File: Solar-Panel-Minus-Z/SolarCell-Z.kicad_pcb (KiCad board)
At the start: 6 copper layers, 48.4 x 48.4 mm, 74 parts, among them J1 XF2M-1015-1A, J2 U.FL-R-SMT-1, Q1 IRLML2803, U1 NDS8434, U2 Value, U3 Value, U4 TTB12G51-Balun

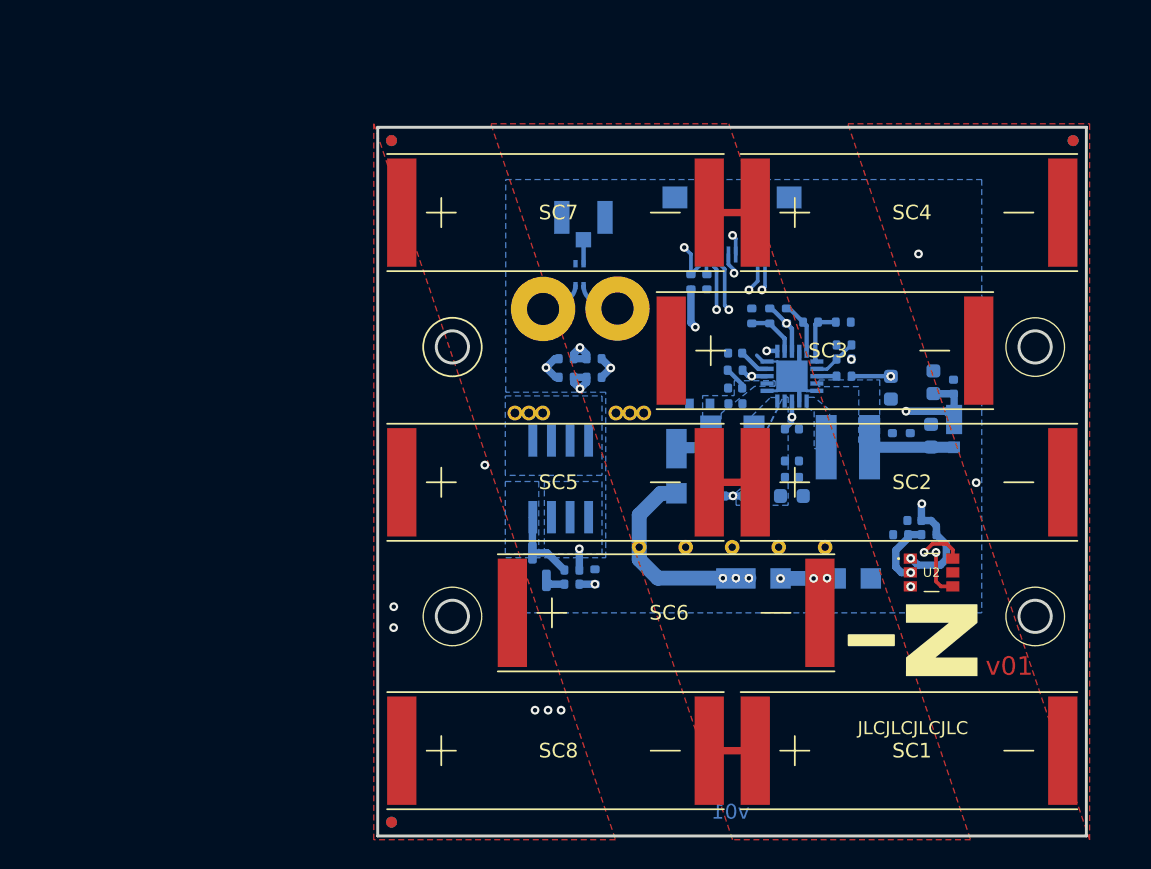
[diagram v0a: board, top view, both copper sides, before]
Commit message: Done with X, +/-Y, and +Z. TODO: -Z
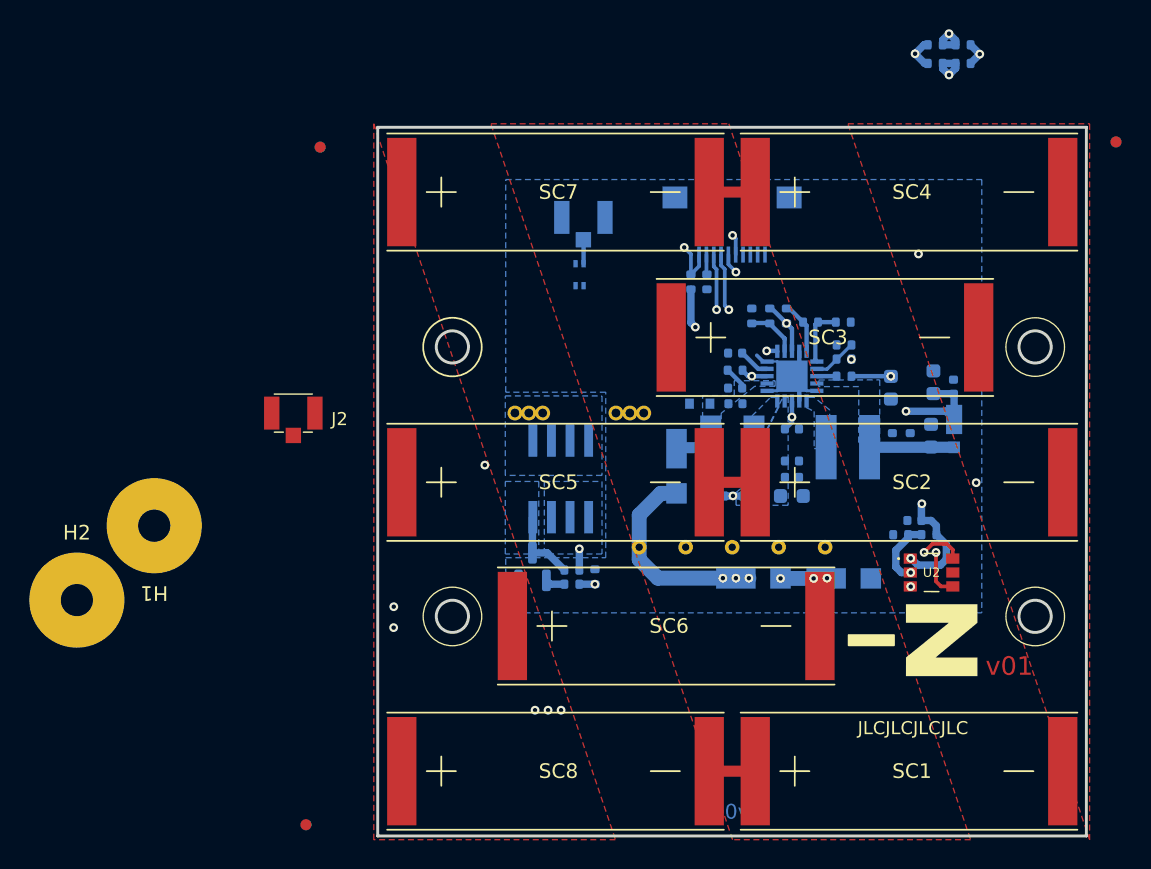
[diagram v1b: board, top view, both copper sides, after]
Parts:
- added J2: U.FL-R-SMT-1, misc-circuits:U.FL-R-SMT-1, F.Cu at (73.2, 60.0)
- H1, H2: footprint MountingHole:MountingHole_2.2mm_M2_Pad -> misc-circuits:Antenna Pad
- moved H2 37.5 mm to (58.4, 72.7), turned to 0 degrees
- moved H1 34.9 mm to (63.7, 67.7)
- moved R17 33.1 mm to (117.0, 34.8)
- moved R18 33.1 mm to (118.9, 34.8)
- moved R12 33.1 mm to (118.9, 36.1)
- moved R13 33.1 mm to (117.0, 36.1)
- moved REF** 5.84 mm to (74.0, 88.1) (x2)
- moved REF** 4.90 mm to (75.0, 41.8) (x2)
- moved REF** 2.93 mm to (129.3, 41.5) (x2)
- moved SC1 1.40 mm to (104.7, 84.4)
- moved SC7 1.40 mm to (80.6, 44.9)
- moved SC8 1.40 mm to (80.6, 84.4)
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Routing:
- net /coil: track 14271.2 -> 3553.6 mm
- net COIL_P: track 22.4 -> 2.83 mm, vias 2 -> 1
- net COIL_N: track 20.3 -> 2.78 mm, vias 2 -> 1
- net +3V3: track 53.4 -> 42.4 mm
- net Net-(H2-Pad1): track 3.19 -> 0.00 mm
- net BURN1: track 35.3 -> 32.2 mm
- net Net-(H1-Pad1): track 3.06 -> 0.00 mm
- net VSOLAR_FULL: track 34.2 -> 32.6 mm

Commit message: -Z board changes
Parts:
- removed the J2 at (93.0, 46.6)
- removed the SC3 at (99.0, 54.8)
- removed the SC6 at (88.1, 74.5)
- added JP2: Jumper, SolarCellParts:Burn-Wire-Rotated, B.Cu at (116.9, 53.7)
- J2: moved to B.Cu
- moved H2 46.6 mm to (103.1, 59.7)
- moved H1 42.2 mm to (103.1, 52.7)
- moved R18 33.9 mm to (112.3, 68.1), turned to 0 degrees
- moved R17 33.4 mm to (114.2, 68.1), turned to 0 degrees
- moved R12 31.5 mm to (112.3, 66.9), turned to 180 degrees
- moved R13 30.9 mm to (114.2, 66.9), turned to 180 degrees
- moved R19 27.0 mm to (113.1, 53.7)
- moved R4 27.0 mm to (113.1, 54.7)
- moved R3 26.2 mm to (114.6, 55.2), turned to -90 degrees
- moved Q1 26.2 mm to (110.4, 54.7)
- moved U1 26.1 mm to (112.3, 48.8)
- moved J2 25.6 mm to (98.4, 55.9), turned to -90 degrees
- moved D3 25.2 mm to (88.9, 58.7), turned to 90 degrees
- moved SC5 22.6 mm to (80.6, 67.5)
- moved SC4 19.8 mm to (80.6, 44.9)
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- renumbered SC4 to SC3, SC5 to SC4, SC7 to SC5, SC8 to SC6
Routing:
- net /coil: track 3553.6 -> 13587.3 mm
- net COIL_N: track 2.78 -> 37.6 mm, vias 1 -> 2
- net COIL_P: track 2.83 -> 35.1 mm, vias 1 -> 2
- net +3V3: track 42.4 -> 58.9 mm
- net VSOLAR_FULL: track 32.6 -> 18.2 mm, vias 6 -> 5
- net BURN1: track 32.2 -> 45.4 mm
- net BATT_P: track 39.1 -> 49.8 mm
- net Net-(D3-Pad1): track 12.5 -> 22.4 mm, vias 3 -> 6
- net Net-(H2-Pad1): track 0.00 -> 3.20 mm
- net Net-(H1-Pad1): track 0.00 -> 3.19 mm
- net /VBAT: track 16.2 -> 18.4 mm
- net SCL1: track 29.7 -> 27.6 mm
- net Net-(R10-Pad2): track 8.94 -> 10.7 mm
- net VOUT_EN: track 12.6 -> 14.2 mm
- net GND: track 9.34 -> 10.4 mm, vias 3 -> 1
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- added copper zone on F.Cu, net Net-(H1-Pad1)
- added copper zone on F.Cu, net Net-(H2-Pad1)
- removed copper zone on B.Cu, net Net-(Q1-Pad3)
